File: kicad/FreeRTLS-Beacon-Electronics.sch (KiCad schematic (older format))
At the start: 22 parts

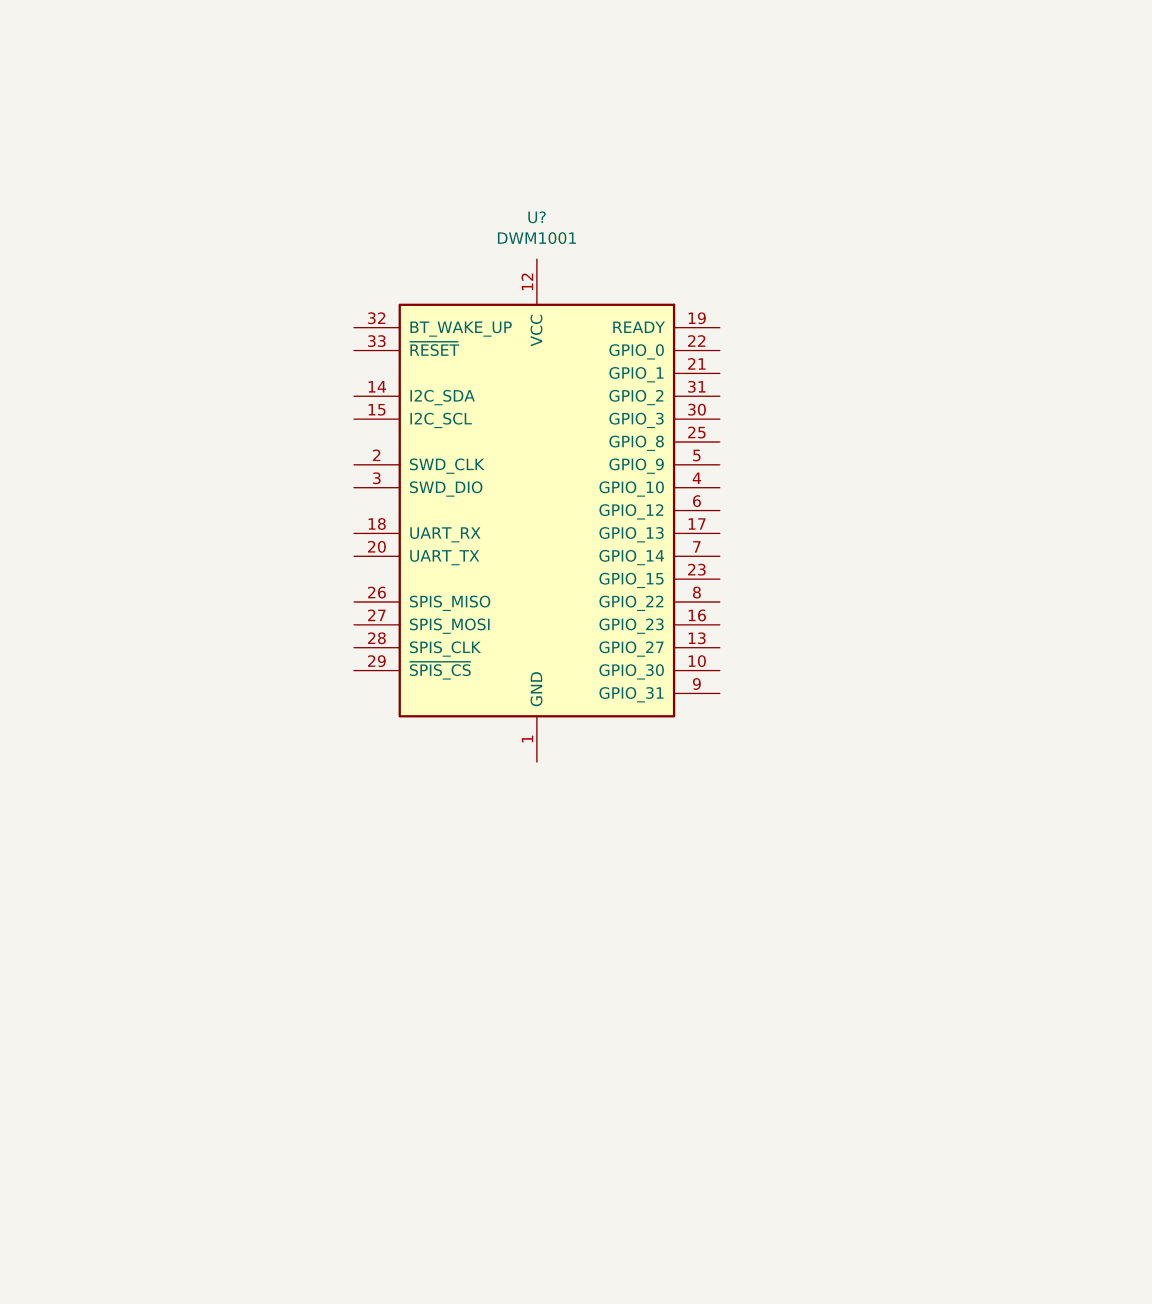
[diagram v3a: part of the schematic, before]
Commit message: Complete DWM1001 section
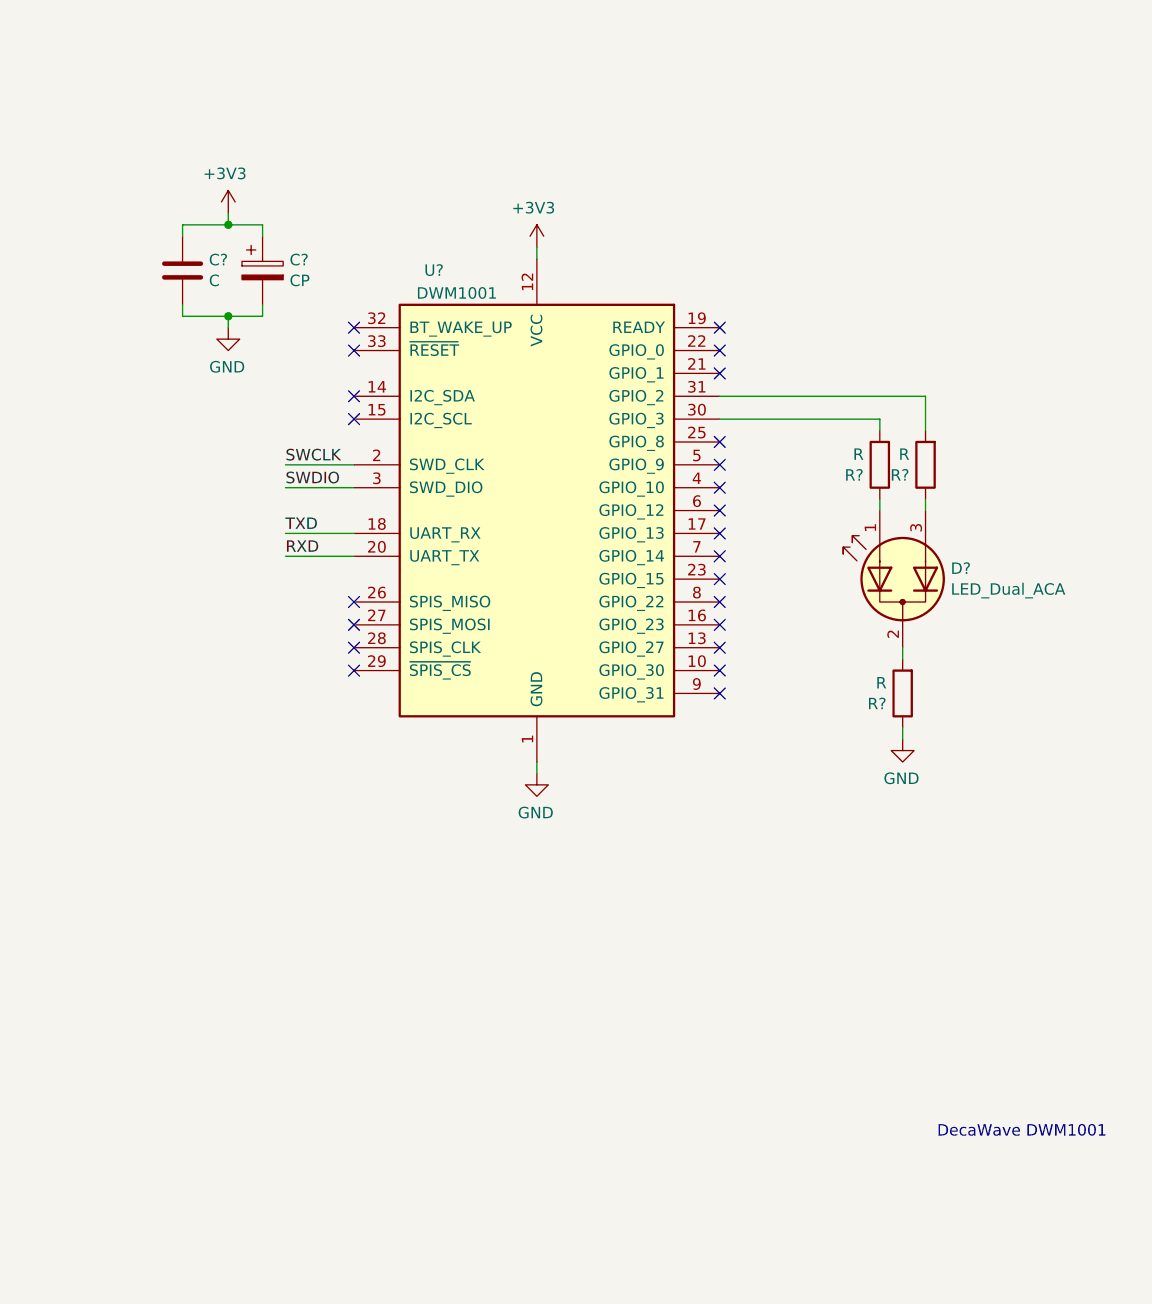
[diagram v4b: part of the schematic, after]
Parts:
- added C?: CP, symbol Device:CP
- added C?: C, symbol Device:C
- added D?: LED_Dual_ACA, symbol Device:LED_Dual_ACA
- added R? (x3): R, symbol Device:R
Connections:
- net +3V3: now also U?.12 (VCC), C?.1, C?.1
- net GND: now also U?.1 (GND), U?.11 (GND), U?.24 (GND), U?.34 (GND), C?.2, C?.2, R?.1
- net RXD: now also U?.20 (UART_TX)
- net SWCLK: now also U?.2 (SWD_CLK)
- net SWDIO: now also U?.3 (SWD_DIO)
- net TXD: now also U?.18 (UART_RX)
- net at U?.30 (GPIO_3): now also R?.2
- net at U?.31 (GPIO_2): now also R?.2
- new net: D?.1 (A1), R?.1
- new net: D?.2 (K), R?.2
- new net: D?.3 (A2), R?.1
- no-connect marks 29 -> 52
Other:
- note added: "DecaWave DWM1001"
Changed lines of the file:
@@
 Sheet 1 1
 Title "FreeRTLS Beacon Electronics"
-Date "2020-09-01"
+Date "2020-09-02"
 Rev "WIP!"
 Comp "FreeRTLS"
@@
 U 1 1 5F4EAC7B
 P 8600 3650
-F 0 "U?" H 8600 4931 50  0000 C CNN
-F 1 "DWM1001" H 8600 4840 50  0000 C CNN
+F 0 "U?" H 8150 4700 50  0000 C CNN
+F 1 "DWM1001" H 8250 4600 50  0000 C CNN
 F 2 "RF_Module:DecaWave_DWM1001" H 9300 2700 50  0001 C CNN
 F 3 "https://www.decawave.com/sites/default/files/dwm1001_datasheet.pdf" H 9500 2850 50  0001 C CNN
@@
 STM_SWCLK
 NoConn ~ 1550 6100
+$Comp
+L power:+3V3 #PWR?
+U 1 1 5F74B660
+P 8600 2500
+F 0 "#PWR?" H 8600 2350 50  0001 C CNN
+F 1 "+3V3" H 8615 2673 50  0000 C CNN
+F 2 "" H 8600 2500 50  0001 C CNN
+F 3 "" H 8600 2500 50  0001 C CNN
+	1    8600 2500
+	-1   0    0    -1
+$EndComp
+$Comp
+L power:GND #PWR?
+U 1 1 5F74C3EA
+P 8600 4800
+F 0 "#PWR?" H 8600 4550 50  0001 C CNN
+F 1 "GND" H 8605 4627 50  0000 C CNN
+F 2 "" H 8600 4800 50  0001 C CNN
+F 3 "" H 8600 4800 50  0001 C CNN
+	1    8600 4800
+	-1   0    0    -1
+$EndComp
+Wire Wire Line
+	8600 4750 8600 4800
+Wire Wire Line
+	8600 2500 8600 2550
+Text Label 7500 3450 0    50   ~ 0
+SWCLK
+Text Label 7500 3550 0    50   ~ 0
+SWDIO
+Wire Wire Line
+	7500 3450 7800 3450
+Wire Wire Line
+	7500 3550 7800 3550
+NoConn ~ 9400 3550
+NoConn ~ 9400 3450
+NoConn ~ 9400 3850
+NoConn ~ 9400 4050
+NoConn ~ 9400 4350
+NoConn ~ 9400 4450
+$Comp
+L Device:LED_Dual_ACA D?
+U 1 1 5F78127A
+P 10200 3950
+F 0 "D?" V 10246 3740 50  0000 R CNN
+F 1 "LED_Dual_ACA" V 10155 3740 50  0000 R CNN
+F 2 "" H 10200 3950 50  0001 C CNN
+F 3 "~" H 10200 3950 50  0001 C CNN
+	1    10200 3950
+	0    -1   -1   0
+$EndComp
+$Comp
+L Device:R R?
+U 1 1 5F782A90
+P 10100 3450
+F 0 "R?" H 10170 3496 50  0000 L CNN
+F 1 "R" H 10170 3405 50  0000 L CNN
+F 2 "" V 10030 3450 50  0001 C CNN
+F 3 "~" H 10100 3450 50  0001 C CNN
+	1    10100 3450
+	-1   0    0    1
+$EndComp
+$Comp
+L Device:R R?
+U 1 1 5F783AC0
+P 10300 3450
+F 0 "R?" H 10370 3496 50  0000 L CNN
+F 1 "R" H 10370 3405 50  0000 L CNN
+F 2 "" V 10230 3450 50  0001 C CNN
+F 3 "~" H 10300 3450 50  0001 C CNN
+	1    10300 3450
+	-1   0    0    1
+$EndComp
+$Comp
+L Device:R R?
+U 1 1 5F78CFC1
+P 10200 4450
+F 0 "R?" H 10270 4496 50  0000 L CNN
+F 1 "R" H 10270 4405 50  0000 L CNN
+F 2 "" V 10130 4450 50  0001 C CNN
+F 3 "~" H 10200 4450 50  0001 C CNN
+	1    10200 4450
+	-1   0    0    1
+$EndComp
+$Comp
+L power:GND #PWR?
+U 1 1 5F78D3EB
+P 10200 4650
+F 0 "#PWR?" H 10200 4400 50  0001 C CNN
+F 1 "GND" H 10205 4477 50  0000 C CNN
+F 2 "" H 10200 4650 50  0001 C CNN
+F 3 "" H 10200 4650 50  0001 C CNN
+	1    10200 4650
+	-1   0    0    -1
+$EndComp
+Wire Wire Line
+	10200 4650 10200 4600
+Wire Wire Line
+	10200 4300 10200 4250
+Wire Wire Line
+	10100 3650 10100 3600
+Wire Wire Line
+	10300 3650 10300 3600
+Wire Wire Line
+	9400 3250 10100 3250
+Wire Wire Line
+	10100 3250 10100 3300
+Wire Wire Line
+	10300 3300 10300 3150
+Wire Wire Line
+	10300 3150 9400 3150
+NoConn ~ 7800 2950
+NoConn ~ 7800 2850
+$Comp
+L Device:CP C?
+U 1 1 5F7B58BA
+P 7400 2600
+F 0 "C?" H 7518 2646 50  0000 L CNN
+F 1 "CP" H 7518 2555 50  0000 L CNN
+F 2 "" H 7438 2450 50  0001 C CNN
+F 3 "~" H 7400 2600 50  0001 C CNN
+	1    7400 2600
+	1    0    0    -1
+$EndComp
+$Comp
+L Device:C C?
+U 1 1 5F7B6CAC
+P 7050 2600
+F 0 "C?" H 7165 2646 50  0000 L CNN
+F 1 "C" H 7165 2555 50  0000 L CNN
+F 2 "" H 7088 2450 50  0001 C CNN
+F 3 "~" H 7050 2600 50  0001 C CNN
+	1    7050 2600
+	1    0    0    -1
+$EndComp
+NoConn ~ 7800 3150
+NoConn ~ 7800 3250
+NoConn ~ 7800 4050
+NoConn ~ 7800 4150
+NoConn ~ 7800 4250
+NoConn ~ 7800 4350
+NoConn ~ 9400 4250
+NoConn ~ 9400 4150
+NoConn ~ 9400 3950
+NoConn ~ 9400 3750
+NoConn ~ 9400 3650
+NoConn ~ 9400 3350
+NoConn ~ 9400 3050
+NoConn ~ 9400 2950
+NoConn ~ 9400 2850
+Text Label 7500 3850 0    50   ~ 0
+RXD
+Wire Wire Line
+	7500 3750 7800 3750
+Wire Wire Line
+	7500 3850 7800 3850
+Text Label 7500 3750 0    50   ~ 0
+TXD
+$Comp
+L power:+3V3 #PWR?
+U 1 1 5F80030A
+P 7250 2350
+F 0 "#PWR?" H 7250 2200 50  0001 C CNN
+F 1 "+3V3" H 7265 2523 50  0000 C CNN
+F 2 "" H 7250 2350 50  0001 C CNN
+F 3 "" H 7250 2350 50  0001 C CNN
+	1    7250 2350
+	-1   0    0    -1
+$EndComp
+Wire Wire Line
+	7050 2450 7050 2400
+Wire Wire Line
+	7050 2400 7250 2400
+Wire Wire Line
+	7400 2400 7400 2450
+Wire Wire Line
+	7250 2350 7250 2400
+Connection ~ 7250 2400
+Wire Wire Line
+	7250 2400 7400 2400
+Wire Wire Line
+	7050 2800 7250 2800
+Wire Wire Line
+	7400 2800 7400 2750
+Wire Wire Line
+	7050 2750 7050 2800
+$Comp
+L power:GND #PWR?
+U 1 1 5F816EEE
+P 7250 2850
+F 0 "#PWR?" H 7250 2600 50  0001 C CNN
+F 1 "GND" H 7255 2677 50  0000 C CNN
+F 2 "" H 7250 2850 50  0001 C CNN
+F 3 "" H 7250 2850 50  0001 C CNN
+	1    7250 2850
+	-1   0    0    -1
+$EndComp
+Wire Wire Line
+	7250 2850 7250 2800
+Connection ~ 7250 2800
+Wire Wire Line
+	7250 2800 7400 2800
+Text Notes 10350 6400 0    50   ~ 0
+DecaWave DWM1001
 $EndSCHEMATC
